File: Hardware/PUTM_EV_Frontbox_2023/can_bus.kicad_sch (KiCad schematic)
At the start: 4 parts, among them U8 MCP2542FDxMF

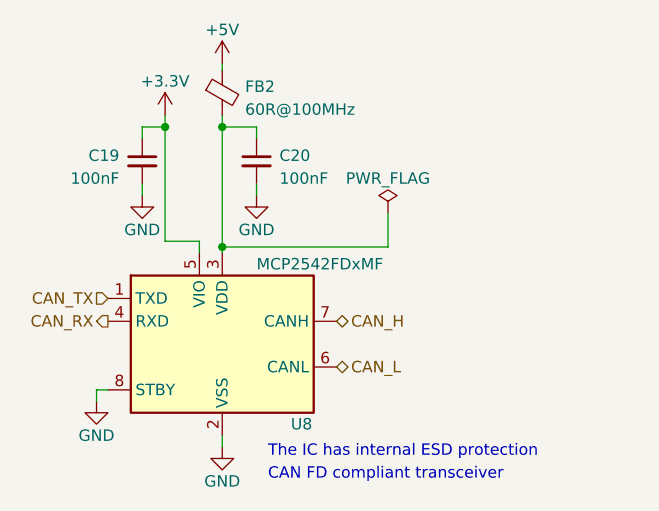
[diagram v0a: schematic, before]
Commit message: Added gearbox temperature sensors on schematic
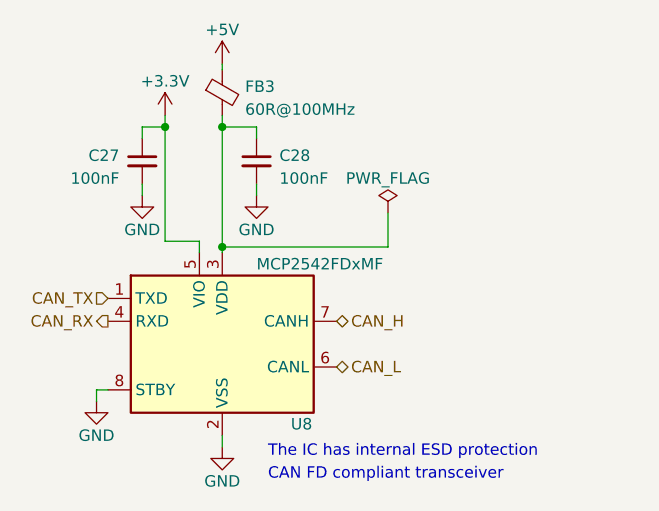
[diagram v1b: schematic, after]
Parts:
- renumbered C19 to C27, C20 to C28, FB2 to FB3
